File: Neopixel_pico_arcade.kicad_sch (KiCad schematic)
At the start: 15 parts, among them J1 SWD_connector, J2 NES_controller_connector, J3 USB_C_Receptacle_USB2.0, Q1 2N7002, U1 RP2040_Stamp, U2 SN74LV1T34DBV, U3 SRV05-4HTG-D

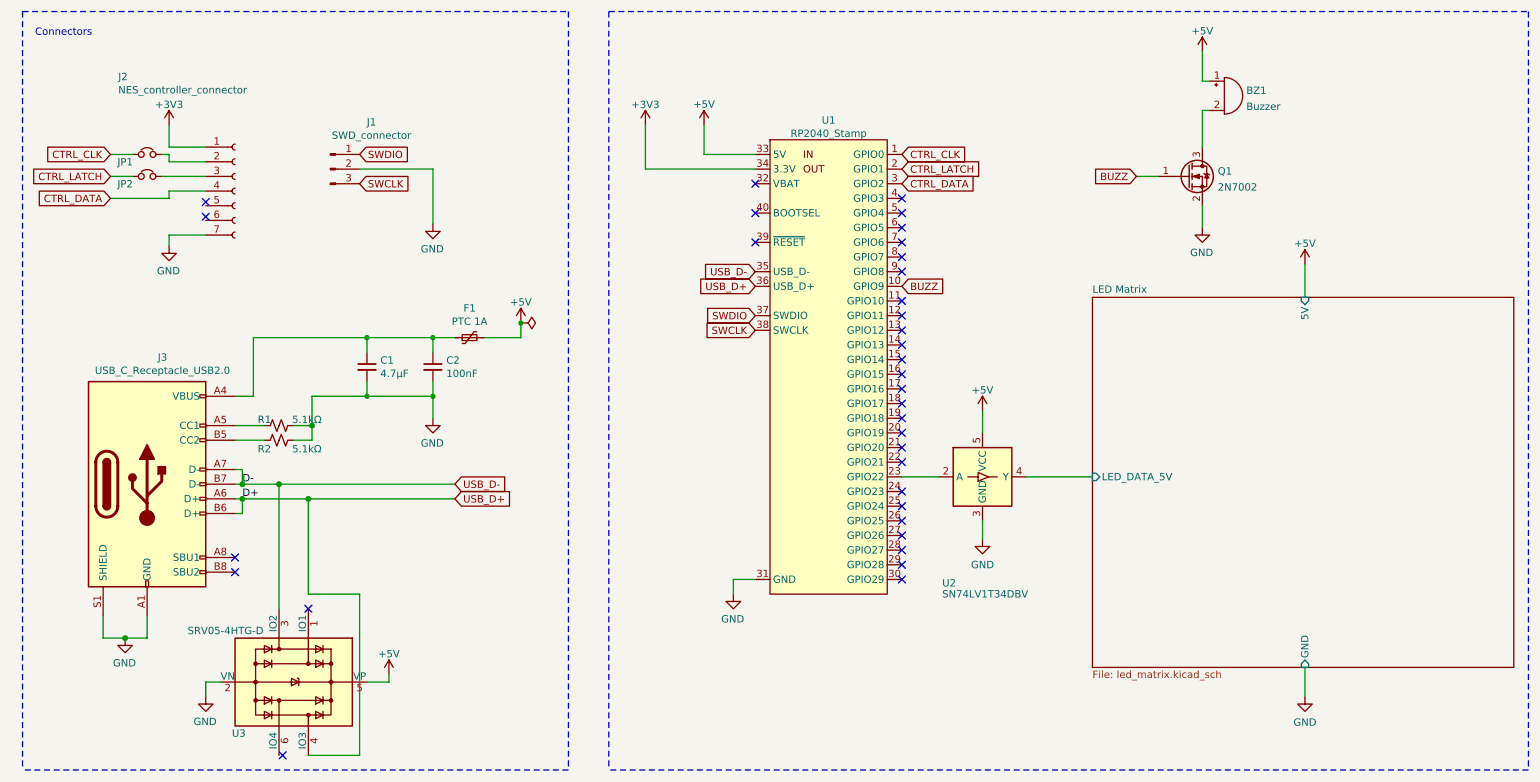
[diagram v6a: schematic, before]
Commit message: Fixes ERC errors on top level sheet
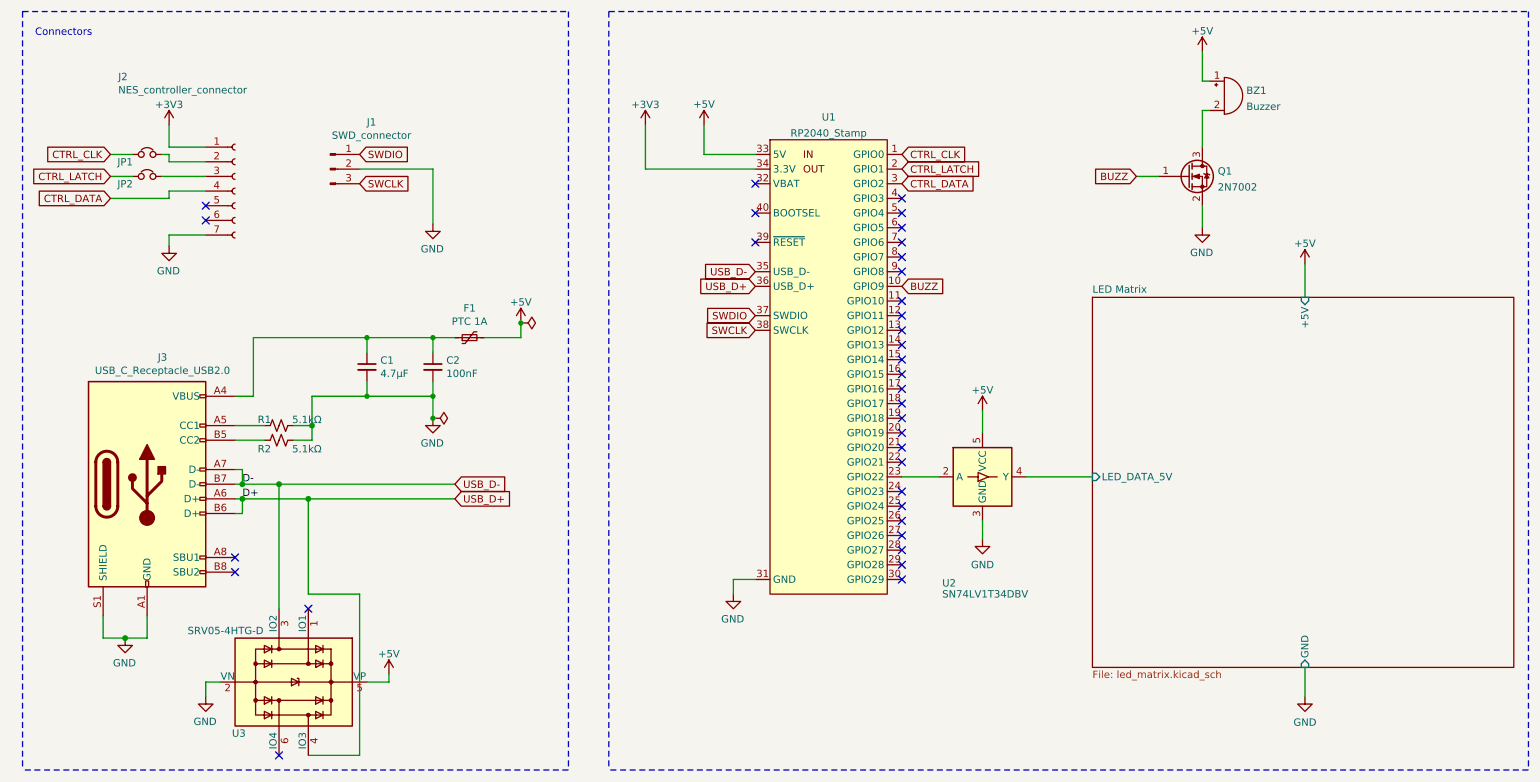
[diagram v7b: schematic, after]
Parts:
- removed U1: RP2040_Stamp, RP2040_Stamp:RP2040_Stamp_SMD, symbol RP2040_Stamp:RP2040_Stamp
- added U1: RP2040_Stamp, RP2040_Stamp:RP2040_Stamp_SMD, symbol RP2040_stamp:RP2040_Stamp
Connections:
- net +3V3: now also U1.34 (3.3V)
- net +5V: now also U1.33 (5V)
- net BUZZ: now also U1.10 (GPIO9)
- net CTRL_CLK: now also U1.1 (GPIO0)
- net CTRL_DATA: now also U1.3 (GPIO2)
- net CTRL_LATCH: now also U1.2 (GPIO1)
- net GND: now also U1.31 (GND)
- net SWCLK: now also U1.38 (SWCLK)
- net SWDIO: now also U1.37 (SWDIO)
- net USB_D+: now also U1.36 (USB_D+)
- net USB_D-: now also U1.35 (USB_D-)
- net at U2.2 (A): now also U1.23 (GPIO22)
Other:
- sheet LED Matrix ports: added +5V; removed 5V
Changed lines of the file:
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@@
   (junction (at 90.17 74.93) (diameter 0) (color 0 0 0 0))
   (junction (at 90.17 85.09) (diameter 0) (color 0 0 0 0))
+  (junction (at 90.17 88.9) (diameter 0) (color 0 0 0 0))
   (junction (at 105.41 72.39) (diameter 0) (color 0 0 0 0))
-  (no_connect (at 50.8 51.435))
-  (no_connect (at 50.8 53.975))
+  (no_connect (at 50.8 52.07))
+  (no_connect (at 50.8 54.61))
   (no_connect (at 55.88 113.03))
   (no_connect (at 55.88 115.57))
-  (no_connect (at 64.135 147.32))
+  (no_connect (at 63.5 147.32))
   (no_connect (at 68.58 121.92))
   (no_connect (at 146.05 48.26))
@@
   (symbol (lib_id "power:+5V") (at 82.55 133.35 0) (unit 1)
     (in_bom yes) (on_board yes) (fields_autoplaced)
-    (property "Reference" "#PWR?" (id 0) (at 82.55 137.16 0)
+    (property "Reference" "#PWR0148" (id 0) (at 82.55 137.16 0)
       (effects (font (size 1.27 1.27)) hide)
     )
@@
   (symbol (lib_id "power:+5V") (at 105.41 72.39 0) (unit 1)
     (in_bom yes) (on_board yes) (fields_autoplaced)
-    (property "Reference" "#PWR?" (id 0) (at 105.41 76.2 0)
+    (property "Reference" "#PWR0149" (id 0) (at 105.41 76.2 0)
       (effects (font (size 1.27 1.27)) hide)
     )
@@
   (symbol (lib_id "power:+5V") (at 137.16 38.1 0) (unit 1)
     (in_bom yes) (on_board yes) (fields_autoplaced)
-    (property "Reference" "#PWR?" (id 0) (at 137.16 41.91 0)
+    (property "Reference" "#PWR0150" (id 0) (at 137.16 41.91 0)
       (effects (font (size 1.27 1.27)) hide)
     )
@@
   (symbol (lib_id "power:+5V") (at 185.42 87.63 0) (unit 1)
     (in_bom yes) (on_board yes) (fields_autoplaced)
-    (property "Reference" "#PWR?" (id 0) (at 185.42 91.44 0)
+    (property "Reference" "#PWR0151" (id 0) (at 185.42 91.44 0)
       (effects (font (size 1.27 1.27)) hide)
     )
@@
   (symbol (lib_id "power:+5V") (at 223.52 25.4 0) (unit 1)
     (in_bom yes) (on_board yes) (fields_autoplaced)
-    (property "Reference" "#PWR?" (id 0) (at 223.52 29.21 0)
+    (property "Reference" "#PWR0152" (id 0) (at 223.52 29.21 0)
       (effects (font (size 1.27 1.27)) hide)
     )
@@
   (symbol (lib_id "power:+5V") (at 241.3 62.23 0) (unit 1)
     (in_bom yes) (on_board yes) (fields_autoplaced)
-    (property "Reference" "#PWR?" (id 0) (at 241.3 66.04 0)
+    (property "Reference" "#PWR0153" (id 0) (at 241.3 66.04 0)
       (effects (font (size 1.27 1.27)) hide)
     )
@@
     )
     (property "Datasheet" "" (id 3) (at 241.3 62.23 0)
+      (effects (font (size 1.27 1.27)) hide)
+    )
+    (pin "1")
+  )
+  (symbol (lib_id "power:PWR_FLAG") (at 90.17 88.9 270) (unit 1)
+    (in_bom yes) (on_board yes)
+    (property "Reference" "#FLG0101" (id 0) (at 92.075 88.9 0)
+      (effects (font (size 1.27 1.27)) hide)
+    )
+    (property "Value" "PWR_FLAG" (id 1) (at 93.345 88.9 90)
+      (effects (font (size 1.27 1.27)) (justify left) hide)
+    )
+    (property "Footprint" "" (id 2) (at 90.17 88.9 0)
+      (effects (font (size 1.27 1.27)) hide)
+    )
+    (property "Datasheet" "~" (id 3) (at 90.17 88.9 0)
       (effects (font (size 1.27 1.27)) hide)
     )
@@
     (pin "S1")
   )
-  (symbol (lib_id "RP2040_Stamp:RP2040_Stamp") (at 158.75 82.55 0) (unit 1)
-    (in_bom yes) (on_board yes)
-    (property "Reference" "U1" (id 0) (at 158.75 37.2576 0))
-    (property "Value" "RP2040_Stamp" (id 1) (at 158.75 39.5563 0))
+  (symbol (lib_id "RP2040_stamp:RP2040_Stamp") (at 158.75 82.55 0) (unit 1)
+    (in_bom yes) (on_board yes) (fields_autoplaced)
+    (property "Reference" "U1" (id 0) (at 158.75 36.7242 0))
+    (property "Value" "RP2040_Stamp" (id 1) (at 158.75 39.4993 0))
     (property "Footprint" "RP2040_Stamp:RP2040_Stamp_SMD" (id 2) (at 158.75 123.19 0)
       (effects (font (size 1.27 1.27)) hide)
@@
       (effects (font (size 1.27 1.27)) (justify left))
     )
-    (pin "5V" input (at 241.3 67.945 90)
+    (pin "+5V" input (at 241.3 67.945 90)
       (effects (font (size 1.27 1.27)) (justify right))
     )
@@
       (reference "#FLG01") (unit 1) (value "PWR_FLAG") (footprint "")
     )
+    (path "/cd1aa0e6-fee8-4465-b8a0-a49fa51cfed7"
+      (reference "#FLG0101") (unit 1) (value "PWR_FLAG") (footprint "")
+    )
     (path "/1729631f-de18-4c58-a71d-335612619424"
       (reference "#PWR02") (unit 1) (value "+3V3") (footprint "")
@@
       (reference "#PWR0147") (unit 1) (value "GND") (footprint "")
     )
+    (path "/6c49b017-7d26-4b31-9203-f7fa6b2a453a"
+      (reference "#PWR0148") (unit 1) (value "+5V") (footprint "")
+    )
     (path "/2d959cc5-b271-4536-9ea7-f39ea9c51a26"
-      (reference "#PWR?") (unit 1) (value "+5V") (footprint "")
+      (reference "#PWR0149") (unit 1) (value "+5V") (footprint "")
     )
     (path "/31716d8f-df2f-4a2f-94b3-681ba3d75057"
-      (reference "#PWR?") (unit 1) (value "+5V") (footprint "")
-    )
-    (path "/6c49b017-7d26-4b31-9203-f7fa6b2a453a"
-      (reference "#PWR?") (unit 1) (value "+5V") (footprint "")
+      (reference "#PWR0150") (unit 1) (value "+5V") (footprint "")
+    )
+    (path "/b58d9025-f559-43a2-8cad-d24d15fa24bc"
+      (reference "#PWR0151") (unit 1) (value "+5V") (footprint "")
     )
     (path "/a1b8871f-612b-4d6e-b819-9768d829e3c8"
-      (reference "#PWR?") (unit 1) (value "+5V") (footprint "")
-    )
-    (path "/b58d9025-f559-43a2-8cad-d24d15fa24bc"
-      (reference "#PWR?") (unit 1) (value "+5V") (footprint "")
+      (reference "#PWR0152") (unit 1) (value "+5V") (footprint "")
     )
     (path "/f5948381-d08e-4743-abc3-ccc0a0ba9733"
-      (reference "#PWR?") (unit 1) (value "+5V") (footprint "")
+      (reference "#PWR0153") (unit 1) (value "+5V") (footprint "")
     )
     (path "/6b2c05fc-325d-47a8-82b6-bd0eb739f2e9"
@@
       (reference "R2") (unit 1) (value "5.1kΩ") (footprint "Resistor_SMD:R_0805_2012Metric_Pad1.20x1.40mm_HandSolder")
     )
-    (path "/a76957cc-c237-40f9-be1a-cf769b98f427"
+    (path "/99fe8e35-e5c1-4239-bd41-6a284ef403a7"
       (reference "U1") (unit 1) (value "RP2040_Stamp") (footprint "RP2040_Stamp:RP2040_Stamp_SMD")
     )

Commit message: Associates most components with footprints
We're still missing the NES controller connector footprint.
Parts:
- BZ1: footprint (none) -> Buzzer_Beeper:MagneticBuzzer_CUI_CMT-8504-100-SMT
- F1: footprint Generative_picture:Belfuse_0ZCJ -> Neopixel_pico_arcade:Belfuse_0ZCJ
- J1: footprint (none) -> Connector_PinHeader_2.54mm:PinHeader_1x03_P2.54mm_Vertical
- J3: footprint Generative_picture:USB_C_Receptacle_JAE_DX07S016JA1 -> Neopixel_pico_arcade:USB_C_Receptacle_JAE_DX07S016JA1
- JP1, JP2: footprint (none) -> Jumper:SolderJumper-2_P1.3mm_Bridged_RoundedPad1.0x1.5mm
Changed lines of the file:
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@@
       (effects (font (size 1.27 1.27)) hide)
     )
-    (property "Footprint" "" (id 2) (at 40.64 43.18 0)
+    (property "Footprint" "Jumper:SolderJumper-2_P1.3mm_Bridged_RoundedPad1.0x1.5mm" (id 2) (at 40.64 43.18 0)
       (effects (font (size 1.27 1.27)) hide)
     )
@@
       (effects (font (size 1.27 1.27)) hide)
     )
-    (property "Footprint" "" (id 2) (at 40.64 46.99 0)
+    (property "Footprint" "Jumper:SolderJumper-2_P1.3mm_Bridged_RoundedPad1.0x1.5mm" (id 2) (at 40.64 46.99 0)
       (effects (font (size 1.27 1.27)) hide)
     )
@@
     (property "Reference" "F1" (id 0) (at 96.52 69.8308 90))
     (property "Value" "PTC 1A" (id 1) (at 96.52 72.13 90))
-    (property "Footprint" "Generative_picture:Belfuse_0ZCJ" (id 2) (at 101.6 73.66 0)
+    (property "Footprint" "Neopixel_pico_arcade:Belfuse_0ZCJ" (id 2) (at 101.6 73.66 0)
       (effects (font (size 1.27 1.27)) (justify left) hide)
     )
@@
     (property "Reference" "J1" (id 0) (at 79.5274 37.5878 0))
     (property "Value" "SWD_connector" (id 1) (at 79.5274 39.8865 0))
-    (property "Footprint" "" (id 2) (at 72.39 45.72 0)
+    (property "Footprint" "Connector_PinHeader_2.54mm:PinHeader_1x03_P2.54mm_Vertical" (id 2) (at 72.39 45.72 0)
       (effects (font (size 1.27 1.27)) hide)
     )
@@
       (effects (font (size 1.27 1.27)) (justify left))
     )
-    (property "Footprint" "" (id 2) (at 226.695 30.48 90)
+    (property "Footprint" "Buzzer_Beeper:MagneticBuzzer_CUI_CMT-8504-100-SMT" (id 2) (at 226.695 30.48 90)
       (effects (font (size 1.27 1.27)) hide)
     )
@@
     (property "Reference" "J3" (id 0) (at 43.307 78.3398 0))
     (property "Value" "USB_C_Receptacle_USB2.0" (id 1) (at 43.307 80.6385 0))
-    (property "Footprint" "Generative_picture:USB_C_Receptacle_JAE_DX07S016JA1" (id 2) (at 44.45 100.33 0)
+    (property "Footprint" "Neopixel_pico_arcade:USB_C_Receptacle_JAE_DX07S016JA1" (id 2) (at 44.45 100.33 0)
       (effects (font (size 1.27 1.27)) hide)
     )
@@
     )
     (path "/6b2c05fc-325d-47a8-82b6-bd0eb739f2e9"
-      (reference "BZ1") (unit 1) (value "Buzzer") (footprint "")
+      (reference "BZ1") (unit 1) (value "Buzzer") (footprint "Buzzer_Beeper:MagneticBuzzer_CUI_CMT-8504-100-SMT")
     )
     (path "/3dcd957e-2bc0-456f-b0ec-92b7bc5b3d89"
@@
     )
     (path "/74305f2c-f10c-4e4c-a8ae-084ce366880f"
-      (reference "F1") (unit 1) (value "PTC 1A") (footprint "Generative_picture:Belfuse_0ZCJ")
+      (reference "F1") (unit 1) (value "PTC 1A") (footprint "Neopixel_pico_arcade:Belfuse_0ZCJ")
     )
     (path "/2d555828-831d-4418-8791-29126d2f97c5"
-      (reference "J1") (unit 1) (value "SWD_connector") (footprint "")
+      (reference "J1") (unit 1) (value "SWD_connector") (footprint "Connector_PinHeader_2.54mm:PinHeader_1x03_P2.54mm_Vertical")
     )
     (path "/2828928c-8c9d-4cab-b139-7b354a50c9ff"
@@
     )
     (path "/6c963e39-9c66-450d-9ace-cb36b00aa8c0"
-      (reference "J3") (unit 1) (value "USB_C_Receptacle_USB2.0") (footprint "Generative_picture:USB_C_Receptacle_JAE_DX07S016JA1")
+      (reference "J3") (unit 1) (value "USB_C_Receptacle_USB2.0") (footprint "Neopixel_pico_arcade:USB_C_Receptacle_JAE_DX07S016JA1")
     )
     (path "/a9c99e6b-55b1-4adc-8611-0aea35c1c656"
-      (reference "JP1") (unit 1) (value "jmp") (footprint "")
+      (reference "JP1") (unit 1) (value "jmp") (footprint "Jumper:SolderJumper-2_P1.3mm_Bridged_RoundedPad1.0x1.5mm")
     )
     (path "/87921a4f-6ae8-4267-b5e7-44fa4718debc"
-      (reference "JP2") (unit 1) (value "jmp") (footprint "")
+      (reference "JP2") (unit 1) (value "jmp") (footprint "Jumper:SolderJumper-2_P1.3mm_Bridged_RoundedPad1.0x1.5mm")
     )
     (path "/691f88c6-2cd2-4539-9dfe-b9f1bc68fc22"
